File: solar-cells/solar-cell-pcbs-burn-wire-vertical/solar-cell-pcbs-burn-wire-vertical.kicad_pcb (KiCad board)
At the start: 2 copper layers, 80 x 103.5 mm, 18 parts, among them J1 Solar Cell, J2 Burn Wire

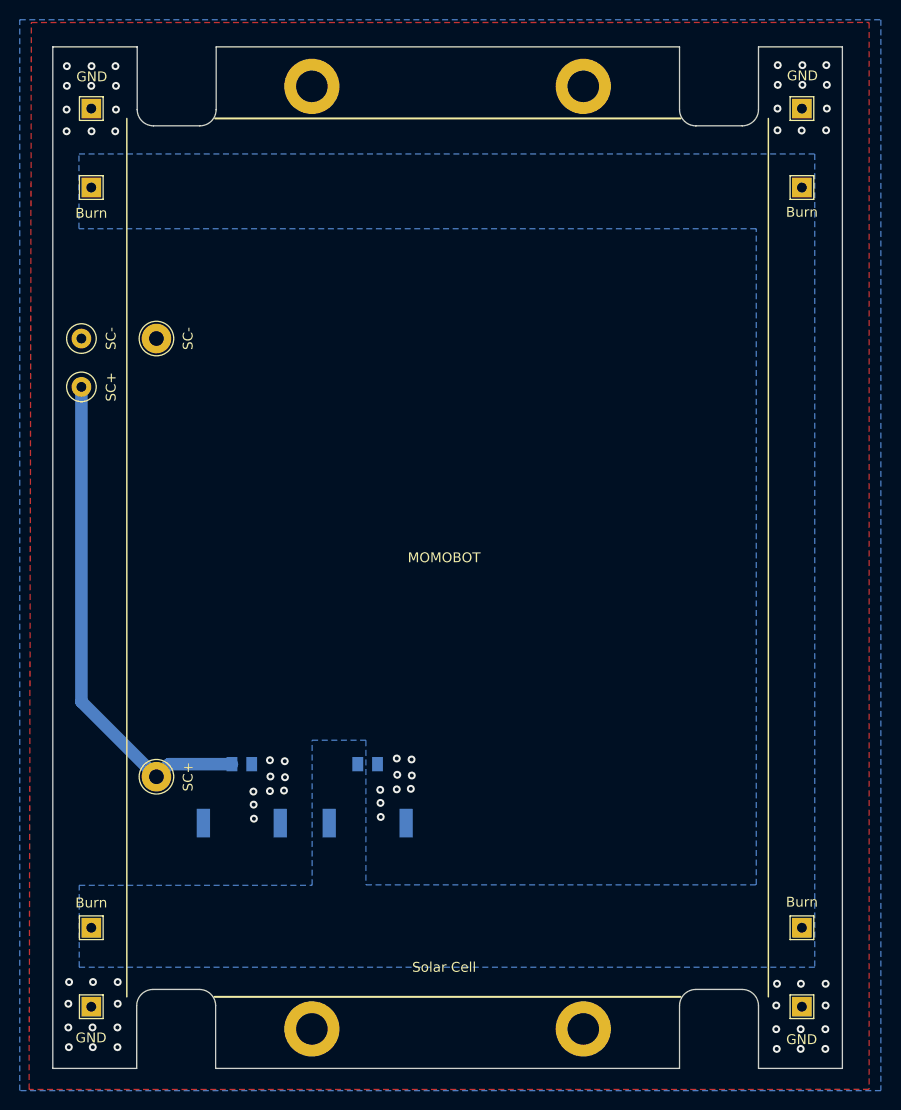
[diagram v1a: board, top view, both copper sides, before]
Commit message: changes to routes in burn wire pcb
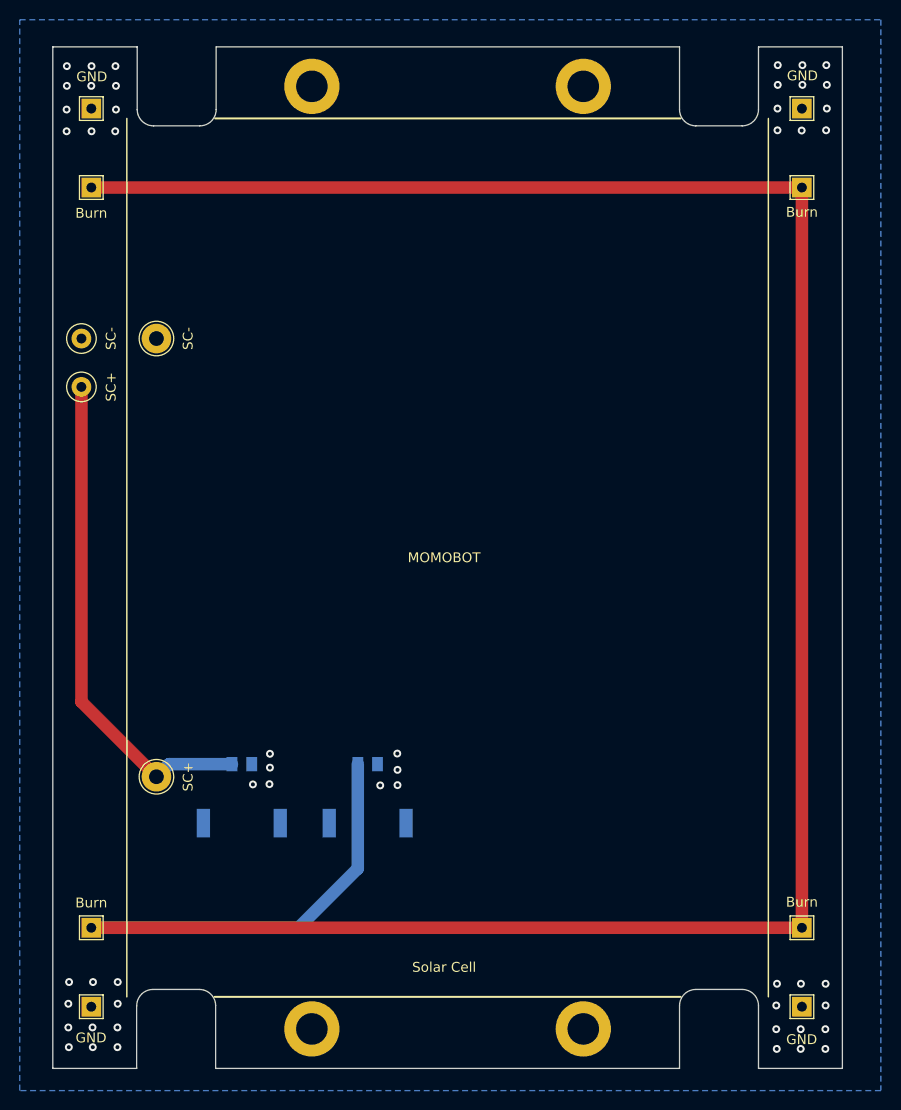
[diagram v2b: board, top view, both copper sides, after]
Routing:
- net BURN: track 0.00 -> 259.1 mm
- net GND: vias 62 -> 52
- removed copper zone on B.Cu, net BURN
- removed copper zone on F.Cu, net GND
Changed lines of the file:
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@@
     (style (thickness 0.15) (arrow_length 1.27) (text_position_mode 0) (extension_height 0.58642) (extension_offset 0.5) keep_text_aligned)
   )
+  (segment (start 75 105.1) (end 82.6 112.7) (width 1.27) (layer "F.Cu") (net 1))
+  (segment (start 75 73.2) (end 75 105.1) (width 1.27) (layer "F.Cu") (net 1))
   (segment (start 83.874999 111.425001) (end 82.6 112.7) (width 1.27) (layer "B.Cu") (net 1))
-  (segment (start 75 105.1) (end 82.6 112.7) (width 1.27) (layer "B.Cu") (net 1))
-  (segment (start 75 73.2) (end 75 105.1) (width 1.27) (layer "B.Cu") (net 1))
   (segment (start 90.253499 111.425001) (end 83.874999 111.425001) (width 1.27) (layer "B.Cu") (net 1))
   (via (at 78.65 140.1) (size 0.8) (drill 0.4) (layers "F.Cu" "B.Cu") (free) (net 2))
@@
   (via (at 150.4 135.875) (size 0.8) (drill 0.4) (layers "F.Cu" "B.Cu") (free) (net 2))
   (via (at 76 42.7) (size 0.8) (drill 0.4) (layers "F.Cu" "B.Cu") (free) (net 2))
-  (via (at 95.6 111.125) (size 0.8) (drill 0.4) (layers "F.Cu" "B.Cu") (free) (net 2))
   (via (at 73.5 47.3) (size 0.8) (drill 0.4) (layers "F.Cu" "B.Cu") (free) (net 2))
   (via (at 73.675 138.1) (size 0.8) (drill 0.4) (layers "F.Cu" "B.Cu") (free) (net 2))
-  (via (at 94.1 111.025) (size 0.8) (drill 0.4) (layers "F.Cu" "B.Cu") (free) (net 2))
+  (via (at 94.1 110.375) (size 0.8) (drill 0.4) (layers "F.Cu" "B.Cu") (free) (net 2))
   (via (at 76.125 138.1) (size 0.8) (drill 0.4) (layers "F.Cu" "B.Cu") (free) (net 2))
   (via (at 78.65 138.1) (size 0.8) (drill 0.4) (layers "F.Cu" "B.Cu") (free) (net 2))
-  (via (at 106.95 110.85) (size 0.8) (drill 0.4) (layers "F.Cu" "B.Cu") (free) (net 2))
+  (via (at 107 110.35) (size 0.8) (drill 0.4) (layers "F.Cu" "B.Cu") (free) (net 2))
   (via (at 78.45 40.7) (size 0.8) (drill 0.4) (layers "F.Cu" "B.Cu") (free) (net 2))
   (via (at 145.55 40.6) (size 0.8) (drill 0.4) (layers "F.Cu" "B.Cu") (free) (net 2))
   (via (at 73.75 133.5) (size 0.8) (drill 0.4) (layers "F.Cu" "B.Cu") (free) (net 2))
   (via (at 150.375 140.275) (size 0.8) (drill 0.4) (layers "F.Cu" "B.Cu") (free) (net 2))
-  (via (at 107 112.5) (size 0.8) (drill 0.4) (layers "F.Cu" "B.Cu") (free) (net 2))
+  (via (at 107.025 112) (size 0.8) (drill 0.4) (layers "F.Cu" "B.Cu") (free) (net 2))
   (via (at 78.675 133.5) (size 0.8) (drill 0.4) (layers "F.Cu" "B.Cu") (free) (net 2))
   (via (at 78.5 45.1) (size 0.8) (drill 0.4) (layers "F.Cu" "B.Cu") (free) (net 2))
-  (via (at 94.1 114.15) (size 0.8) (drill 0.4) (layers "F.Cu" "B.Cu") (free) (net 2))
-  (via (at 106.95 113.975) (size 0.8) (drill 0.4) (layers "F.Cu" "B.Cu") (free) (net 2))
+  (via (at 94.05 113.45) (size 0.8) (drill 0.4) (layers "F.Cu" "B.Cu") (free) (net 2))
+  (via (at 107.025 113.55) (size 0.8) (drill 0.4) (layers "F.Cu" "B.Cu") (free) (net 2))
   (via (at 73.525 40.7) (size 0.8) (drill 0.4) (layers "F.Cu" "B.Cu") (free) (net 2))
   (via (at 150.475 40.6) (size 0.8) (drill 0.4) (layers "F.Cu" "B.Cu") (free) (net 2))
-  (via (at 108.375 113.925) (size 0.8) (drill 0.4) (layers "F.Cu" "B.Cu") (free) (net 2))
   (via (at 150.4 133.675) (size 0.8) (drill 0.4) (layers "F.Cu" "B.Cu") (free) (net 2))
-  (via (at 108.475 112.575) (size 0.8) (drill 0.4) (layers "F.Cu" "B.Cu") (free) (net 2))
   (via (at 150.375 138.275) (size 0.8) (drill 0.4) (layers "F.Cu" "B.Cu") (free) (net 2))
   (via (at 76.025 40.7) (size 0.8) (drill 0.4) (layers "F.Cu" "B.Cu") (free) (net 2))
   (via (at 147.9 133.675) (size 0.8) (drill 0.4) (layers "F.Cu" "B.Cu") (free) (net 2))
-  (via (at 94.15 112.675) (size 0.8) (drill 0.4) (layers "F.Cu" "B.Cu") (free) (net 2))
+  (via (at 94.1 111.775) (size 0.8) (drill 0.4) (layers "F.Cu" "B.Cu") (free) (net 2))
   (via (at 150.525 45) (size 0.8) (drill 0.4) (layers "F.Cu" "B.Cu") (free) (net 2))
   (via (at 78.5 42.7) (size 0.8) (drill 0.4) (layers "F.Cu" "B.Cu") (free) (net 2))
@@
   (via (at 78.675 135.7) (size 0.8) (drill 0.4) (layers "F.Cu" "B.Cu") (free) (net 2))
   (via (at 73.675 135.7) (size 0.8) (drill 0.4) (layers "F.Cu" "B.Cu") (free) (net 2))
-  (via (at 92.475 116.95) (size 0.8) (drill 0.4) (layers "F.Cu" "B.Cu") (free) (net 2))
   (via (at 148.05 40.6) (size 0.8) (drill 0.4) (layers "F.Cu" "B.Cu") (free) (net 2))
   (via (at 145.4 135.875) (size 0.8) (drill 0.4) (layers "F.Cu" "B.Cu") (free) (net 2))
   (via (at 73.5 45.1) (size 0.8) (drill 0.4) (layers "F.Cu" "B.Cu") (free) (net 2))
-  (via (at 95.525 114.1) (size 0.8) (drill 0.4) (layers "F.Cu" "B.Cu") (free) (net 2))
   (via (at 148.05 42.6) (size 0.8) (drill 0.4) (layers "F.Cu" "B.Cu") (free) (net 2))
-  (via (at 92.45 115.525) (size 0.8) (drill 0.4) (layers "F.Cu" "B.Cu") (free) (net 2))
-  (via (at 105.325 116.775) (size 0.8) (drill 0.4) (layers "F.Cu" "B.Cu") (free) (net 2))
   (via (at 150.45 47.2) (size 0.8) (drill 0.4) (layers "F.Cu" "B.Cu") (free) (net 2))
-  (via (at 108.45 110.95) (size 0.8) (drill 0.4) (layers "F.Cu" "B.Cu") (free) (net 2))
-  (via (at 105.3 115.35) (size 0.8) (drill 0.4) (layers "F.Cu" "B.Cu") (free) (net 2))
-  (via (at 92.425 114.2) (size 0.8) (drill 0.4) (layers "F.Cu" "B.Cu") (free) (net 2))
-  (via (at 95.625 112.75) (size 0.8) (drill 0.4) (layers "F.Cu" "B.Cu") (free) (net 2))
+  (via (at 92.375 113.475) (size 0.8) (drill 0.4) (layers "F.Cu" "B.Cu") (free) (net 2))
   (via (at 76.175 133.5) (size 0.8) (drill 0.4) (layers "F.Cu" "B.Cu") (free) (net 2))
   (via (at 147.975 47.225) (size 0.8) (drill 0.4) (layers "F.Cu" "B.Cu") (free) (net 2))
-  (via (at 105.275 114.025) (size 0.8) (drill 0.4) (layers "F.Cu" "B.Cu") (free) (net 2))
-  (zone (net 2) (net_name "GND") (layer "F.Cu") (hatch edge 0.508)
-    (connect_pads (clearance 0.508))
-    (min_thickness 0.254) (filled_areas_thickness no)
-    (fill yes (thermal_gap 0.508) (thermal_bridge_width 0.508))
-    (polygon
-      (pts
-        (xy 154.799302 144.375328)
-        (xy 69.701357 144.387619)
-        (xy 69.927809 36.287369)
-        (xy 154.800754 36.275078)
-      )
-    )
-  )
+  (via (at 105.275 113.575) (size 0.8) (drill 0.4) (layers "F.Cu" "B.Cu") (free) (net 2))
+  (segment (start 76 128) (end 148 128) (width 1.27) (layer "F.Cu") (net 3))
+  (segment (start 148 128) (end 148 53) (width 1.27) (layer "F.Cu") (net 3))
+  (segment (start 148 53) (end 76 53) (width 1.27) (layer "F.Cu") (net 3))
+  (segment (start 102.999999 122.000001) (end 97 128) (width 1.27) (layer "B.Cu") (net 3))
+  (segment (start 102.999999 111.425001) (end 102.999999 122.000001) (width 1.27) (layer "B.Cu") (net 3))
+  (segment (start 97 128) (end 76 128) (width 1.27) (layer "B.Cu") (net 3))
   (zone (net 2) (net_name "GND") (layer "B.Cu") (hatch edge 0.508)
     (connect_pads (clearance 0.508))
@@
       )
     )
-  )
-  (zone (net 3) (net_name "BURN") (layer "B.Cu") (hatch edge 0.508)
-    (priority 6)
-    (connect_pads (clearance 0.508))
-    (min_thickness 0.254) (filled_areas_thickness no)
-    (fill yes (thermal_gap 0.508) (thermal_bridge_width 0.508))
-    (polygon
-      (pts
-        (xy 149.3 132)
-        (xy 74.775 132)
-        (xy 74.775 123.7)
-        (xy 98.375 123.7)
-        (xy 98.375 109)
-        (xy 103.825 109)
-        (xy 103.825 123.65)
-        (xy 143.375 123.65)
-        (xy 143.375 57.175)
-        (xy 74.75 57.175)
-        (xy 74.75 49.6)
-        (xy 149.3 49.6)
-      )
-    )
